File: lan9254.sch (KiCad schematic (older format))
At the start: 36 parts, among them U2301 lan9254, X2301 FNETHE025

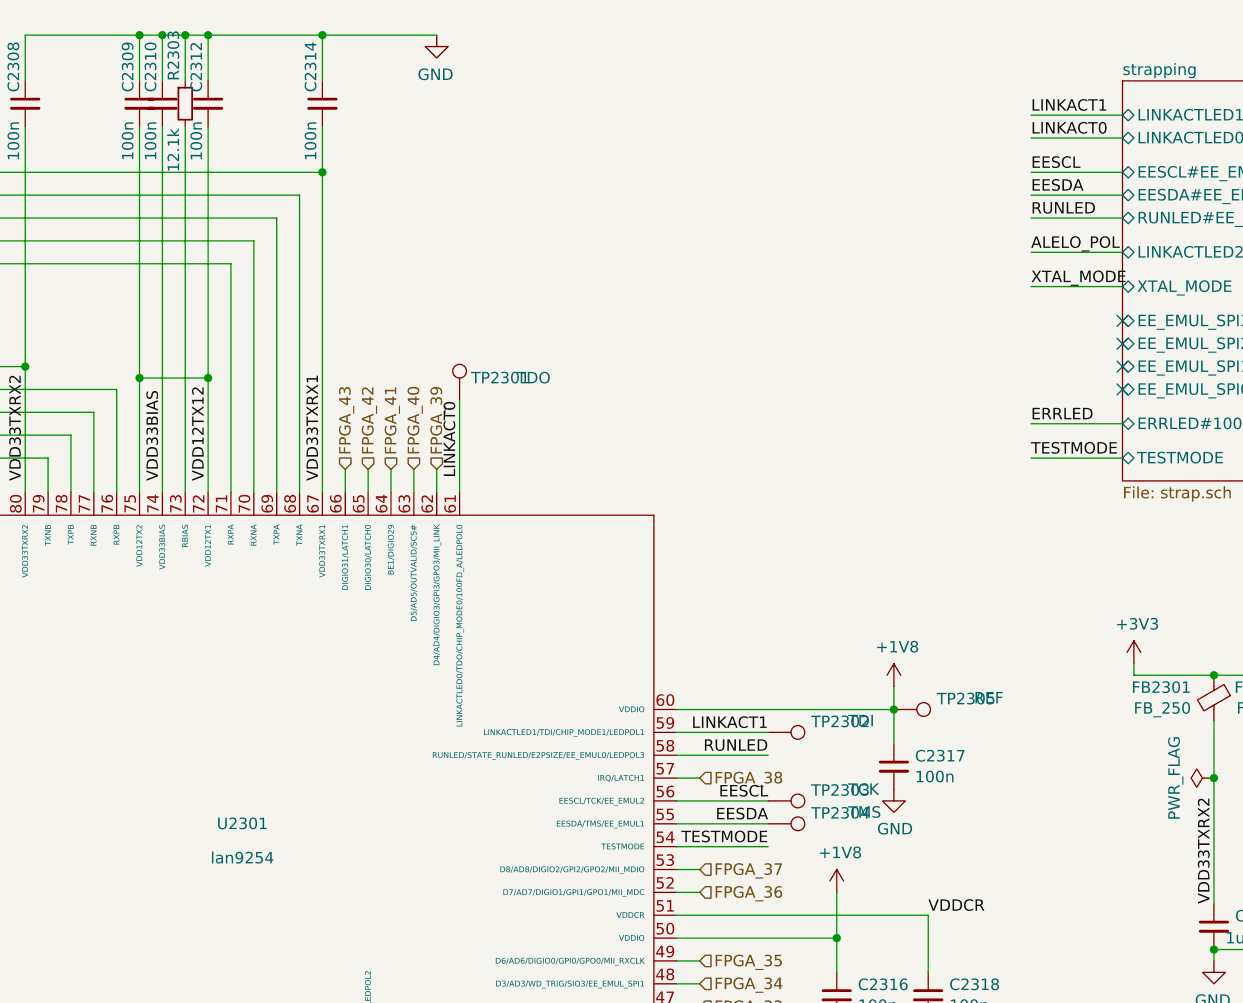
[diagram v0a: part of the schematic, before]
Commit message: fixed i2c switch (Vref2 is *not* a normal power input); small fixes
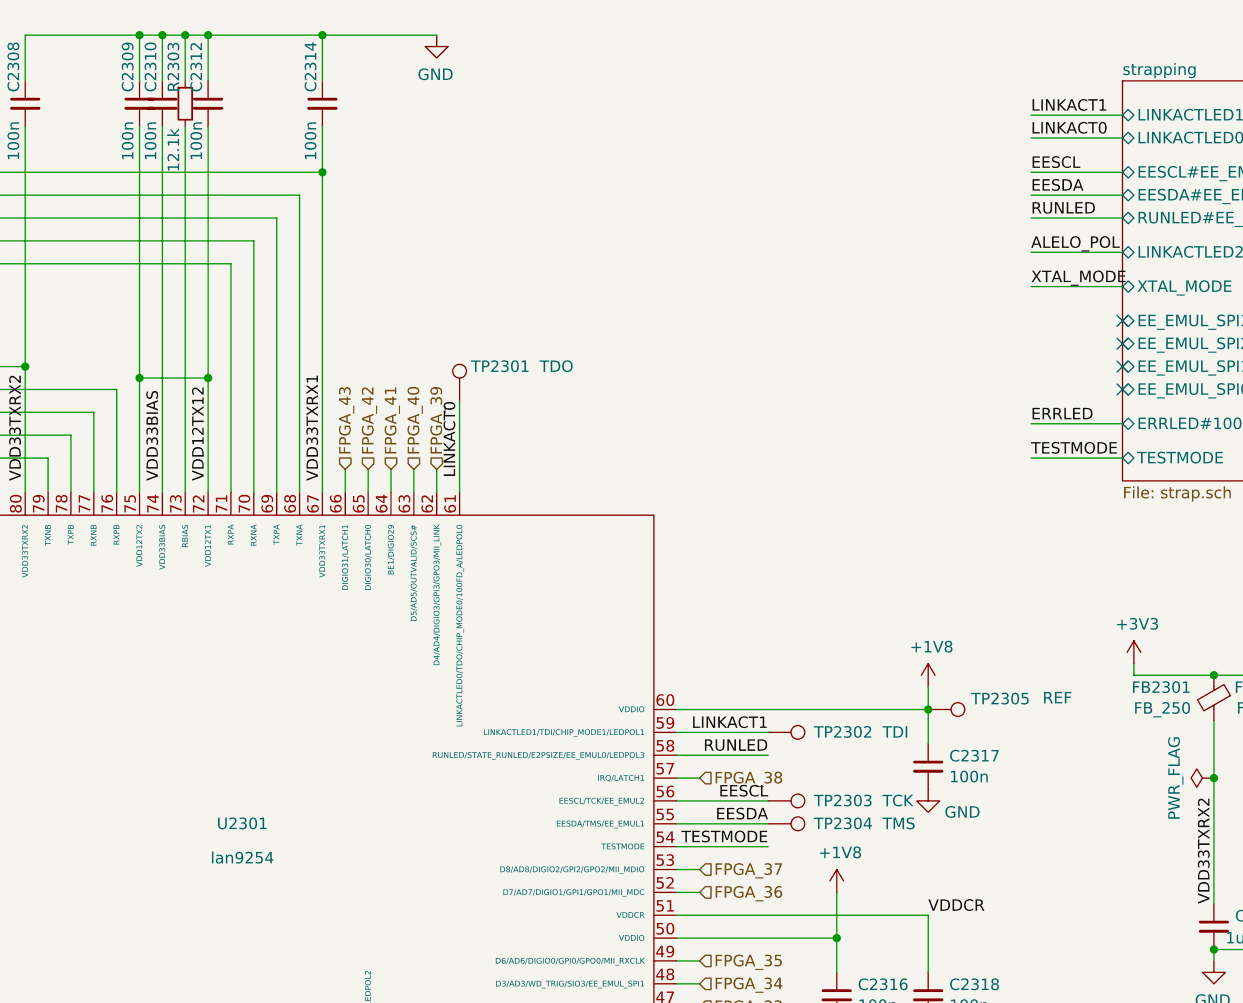
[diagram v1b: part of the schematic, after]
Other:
- moved on the sheet: C2317, TP2305
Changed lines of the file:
@@
 $Descr A4 11693 8268
 encoding utf-8
-Sheet 7 11
+Sheet 7 12
 Title ""
 Date ""
@@
 L Device:C_Small C2317
 U 1 1 60E78D0A
-P 7900 3800
-F 0 "C2317" H 7992 3846 50  0000 L CNN
-F 1 "100n" H 7992 3755 50  0000 L CNN
-F 2 "Capacitor_SMD:C_0402_1005Metric" H 7900 3800 50  0001 C CNN
-F 3 "~" H 7900 3800 50  0001 C CNN
-	1    7900 3800
+P 8050 3800
+F 0 "C2317" H 8142 3846 50  0000 L CNN
+F 1 "100n" H 8142 3755 50  0000 L CNN
+F 2 "Capacitor_SMD:C_0402_1005Metric" H 8050 3800 50  0001 C CNN
+F 3 "~" H 8050 3800 50  0001 C CNN
+	1    8050 3800
 	1    0    0    -1
 $EndComp
@@
 L lan9254_project:GND #PWR?
 U 1 1 60E78EE6
-P 7900 3900
+P 8050 3900
 AR Path="/60DC28BD/60E78EE6" Ref="#PWR?"  Part="1"
 AR Path="/60E78EE6" Ref="#PWR?"  Part="1"
 AR Path="/60DB2574/60E78EE6" Ref="#PWR?"  Part="1"
 AR Path="/60E70F2C/60E78EE6" Ref="#PWR?"  Part="1"
-F 0 "#PWR?" H 7900 3650 50  0001 C CNN
-F 1 "GND" H 7905 3727 50  0000 C CNN
-F 2 "" H 7900 3900 50  0001 C CNN
-F 3 "" H 7900 3900 50  0001 C CNN
-	1    7900 3900
-	1    0    0    -1
-$EndComp
-Wire Wire Line
-	7900 3550 7900 3700
+F 0 "#PWR?" H 8050 3650 50  0001 C CNN
+F 1 "GND" H 8200 3800 50  0000 C CNN
+F 2 "" H 8050 3900 50  0001 C CNN
+F 3 "" H 8050 3900 50  0001 C CNN
+	1    8050 3900
+	1    0    0    -1
+$EndComp
+Wire Wire Line
+	8050 3550 8050 3700
 $Comp
 L Device:C_Small C2307
@@
 L lan9254_project:+1V8 #PWR?
 U 1 1 60E92892
-P 7900 3450
+P 8050 3450
 AR Path="/60DC28BD/60E92892" Ref="#PWR?"  Part="1"
 AR Path="/60E92892" Ref="#PWR?"  Part="1"
 AR Path="/60DB2574/60E92892" Ref="#PWR?"  Part="1"
 AR Path="/60E70F2C/60E92892" Ref="#PWR?"  Part="1"
-F 0 "#PWR?" H 7900 3300 50  0001 C CNN
-F 1 "+1V8" H 7915 3623 50  0000 C CNN
-F 2 "" H 7900 3450 50  0001 C CNN
-F 3 "" H 7900 3450 50  0001 C CNN
-	1    7900 3450
-	1    0    0    -1
-$EndComp
-Wire Wire Line
-	7900 3450 7900 3550
-Connection ~ 7900 3550
+F 0 "#PWR?" H 8050 3300 50  0001 C CNN
+F 1 "+1V8" H 8065 3623 50  0000 C CNN
+F 2 "" H 8050 3450 50  0001 C CNN
+F 3 "" H 8050 3450 50  0001 C CNN
+	1    8050 3450
+	1    0    0    -1
+$EndComp
+Wire Wire Line
+	8050 3450 8050 3550
+Connection ~ 8050 3550
 $Comp
 L Device:C_Small C2306
@@
 AR Path="/60DB2574/60FA54A5" Ref="R2303"  Part="1"
 AR Path="/60E70F2C/60FA54A5" Ref="R2303"  Part="1"
-F 0 "R2303" V 4750 1000 50  0000 L CNN
+F 0 "R2303" V 4750 950 50  0000 L CNN
 F 1 "12.1k" V 4750 600 50  0000 L CNN
 F 2 "Resistor_SMD:R_0603_1608Metric" H 4800 900 50  0001 C CNN
@@
 U 1 1 60E57CD1
 P 6000 2200
-F 0 "TP2301" H 6050 2300 50  0000 L CNN
-F 1 "TDO" H 6250 2300 50  0000 L CNN
+F 0 "TP2301" H 6050 2350 50  0000 L CNN
+F 1 "TDO" H 6350 2350 50  0000 L CNN
 F 2 "Connector_PinHeader_1.27mm:PinHeader_1x01_P1.27mm_Vertical" H 6200 2200 50  0001 C CNN
 F 3 "~" H 6200 2200 50  0001 C CNN
@@
 U 1 1 60E58942
 P 7350 3650
-F 0 "TP2302" V 7304 3838 50  0000 L CNN
-F 1 "TDI" V 7300 4000 50  0000 L CNN
+F 0 "TP2302" V 7350 3850 50  0000 L CNN
+F 1 "TDI" V 7350 4150 50  0000 L CNN
 F 2 "Connector_PinHeader_1.27mm:PinHeader_1x01_P1.27mm_Vertical" H 7550 3650 50  0001 C CNN
 F 3 "~" H 7550 3650 50  0001 C CNN
@@
 	7650 4550 7650 4350
 Connection ~ 7650 4550
-Wire Wire Line
-	6950 3550 7900 3550
 $Comp
 L Connector:TestPoint TP2303
 U 1 1 60E83DE3
 P 7350 3950
-F 0 "TP2303" V 7304 4138 50  0000 L CNN
-F 1 "TCK" V 7300 4300 50  0000 L CNN
+F 0 "TP2303" V 7350 4150 50  0000 L CNN
+F 1 "TCK" V 7350 4450 50  0000 L CNN
 F 2 "Connector_PinHeader_1.27mm:PinHeader_1x01_P1.27mm_Vertical" H 7550 3950 50  0001 C CNN
 F 3 "~" H 7550 3950 50  0001 C CNN
@@
 U 1 1 60E841F7
 P 7350 4050
-F 0 "TP2304" V 7304 4238 50  0000 L CNN
-F 1 "TMS" V 7300 4400 50  0000 L CNN
+F 0 "TP2304" V 7350 4250 50  0000 L CNN
+F 1 "TMS" V 7350 4550 50  0000 L CNN
 F 2 "Connector_PinHeader_1.27mm:PinHeader_1x01_P1.27mm_Vertical" H 7550 4050 50  0001 C CNN
 F 3 "~" H 7550 4050 50  0001 C CNN
@@
 L Connector:TestPoint TP2305
 U 1 1 60E8477A
-P 7900 3550
-F 0 "TP2305" V 7854 3738 50  0000 L CNN
-F 1 "REF" V 7850 3900 50  0000 L CNN
-F 2 "Connector_PinHeader_1.27mm:PinHeader_1x01_P1.27mm_Vertical" H 8100 3550 50  0001 C CNN
-F 3 "~" H 8100 3550 50  0001 C CNN
-	1    7900 3550
+P 8050 3550
+F 0 "TP2305" V 8004 3738 50  0000 L CNN
+F 1 "REF" V 8000 4050 50  0000 L CNN
+F 2 "Connector_PinHeader_1.27mm:PinHeader_1x01_P1.27mm_Vertical" H 8250 3550 50  0001 C CNN
+F 3 "~" H 8250 3550 50  0001 C CNN
+	1    8050 3550
 	0    1    1    0
 $EndComp
+Wire Wire Line
+	6950 3550 8050 3550
 $EndSCHEMATC

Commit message: added more component values/part numbers
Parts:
- FB2301, FB2303, FB2304, FB4: Manufacturer (none) -> TDK
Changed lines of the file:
@@
 F 3 "~" H 9400 5350 50  0001 C CNN
 F 4 "MPZ1608S221ATA00" H 9400 5350 50  0001 C CNN "Part"
+F 5 "TDK" H 9400 5350 50  0001 C CNN "Manufacturer"
 	1    9400 5350
 	0    1    -1   0
@@
 F 3 "~" H 9300 3500 50  0001 C CNN
 F 4 "MPZ1608S221ATA00" H 9300 3500 50  0001 C CNN "Part"
+F 5 "TDK" H 9300 3500 50  0001 C CNN "Manufacturer"
 	1    9300 3500
 	-1   0    0    -1
@@
 F 3 "~" H 9750 3500 50  0001 C CNN
 F 4 "MPZ1608S221ATA00" H 9750 3500 50  0001 C CNN "Part"
+F 5 "TDK" H 9750 3500 50  0001 C CNN "Manufacturer"
 	1    9750 3500
 	-1   0    0    -1
@@
 F 3 "~" H 10200 3500 50  0001 C CNN
 F 4 "MPZ1608S221ATA00" H 10200 3500 50  0001 C CNN "Part"
+F 5 "TDK" H 10200 3500 50  0001 C CNN "Manufacturer"
 	1    10200 3500
 	-1   0    0    -1

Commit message: WIP save
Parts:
- added C2323: 100n, Capacitor_SMD:C_0603_1608Metric, symbol Device:C_Small
- added R2304: 50, Resistor_SMD:R_0603_1608Metric, symbol Device:R_Small
- added U2302: SN74LV1T34DBV, Package_TO_SOT_SMD:SOT-23-5, symbol Logic_LevelTranslator:SN74LV1T34DBV
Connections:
- net labels added: CLK_25MHz, CLK_25_VCC
- wire segments 195 -> 203
- no-connect marks 6 -> 7
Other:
- moved on the sheet: C2301, C2304
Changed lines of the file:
@@
 $Descr A4 11693 8268
 encoding utf-8
-Sheet 7 12
+Sheet 4 18
 Title ""
 Date ""
@@
 	1650 5400 1650 5450
 Wire Wire Line
-	1650 5450 2050 5450
+	1650 5450 1800 5450
 Connection ~ 2050 5450
 Wire Wire Line
@@
 L Device:C_Small C2304
 U 1 1 60EF9CC1
-P 1650 6250
-F 0 "C2304" H 1450 6300 50  0000 L CNN
-F 1 "1u_loESR" H 1250 6200 50  0000 L CNN
-F 2 "Capacitor_SMD:C_0603_1608Metric" H 1650 6250 50  0001 C CNN
-F 3 "~" H 1650 6250 50  0001 C CNN
-	1    1650 6250
+P 10950 5800
+F 0 "C2304" H 10750 5850 50  0000 L CNN
+F 1 "1u_loESR" H 10550 5750 50  0000 L CNN
+F 2 "Capacitor_SMD:C_0603_1608Metric" H 10950 5800 50  0001 C CNN
+F 3 "~" H 10950 5800 50  0001 C CNN
+	1    10950 5800
 	1    0    0    -1
 $EndComp
@@
 L lan9254_project:GND #PWR?
 U 1 1 60EFA87D
-P 1650 6450
+P 10950 6000
 AR Path="/60DC28BD/60EFA87D" Ref="#PWR?"  Part="1"
 AR Path="/60EFA87D" Ref="#PWR?"  Part="1"
 AR Path="/60DB2574/60EFA87D" Ref="#PWR?"  Part="1"
 AR Path="/60E70F2C/60EFA87D" Ref="#PWR?"  Part="1"
-F 0 "#PWR?" H 1650 6200 50  0001 C CNN
-F 1 "GND" H 1655 6277 50  0000 C CNN
-F 2 "" H 1650 6450 50  0001 C CNN
-F 3 "" H 1650 6450 50  0001 C CNN
-	1    1650 6450
+F 0 "#PWR?" H 10950 5750 50  0001 C CNN
+F 1 "GND" H 10955 5827 50  0000 C CNN
+F 2 "" H 10950 6000 50  0001 C CNN
+F 3 "" H 10950 6000 50  0001 C CNN
+	1    10950 6000
 	-1   0    0    -1
 $EndComp
 Wire Wire Line
-	1650 6350 1650 6450
+	10950 5900 10950 6000
 $Comp
 L lan9254_project:+3V3 #PWR?
 U 1 1 60F00E50
-P 1650 6050
+P 10950 5600
 AR Path="/60DC28BD/60F00E50" Ref="#PWR?"  Part="1"
 AR Path="/60F00E50" Ref="#PWR?"  Part="1"
 AR Path="/60DB2574/60F00E50" Ref="#PWR?"  Part="1"
 AR Path="/60E70F2C/60F00E50" Ref="#PWR?"  Part="1"
-F 0 "#PWR?" H 1650 5900 50  0001 C CNN
-F 1 "+3V3" H 1665 6223 50  0000 C CNN
-F 2 "" H 1650 6050 50  0001 C CNN
-F 3 "" H 1650 6050 50  0001 C CNN
-	1    1650 6050
-	1    0    0    -1
-$EndComp
-Wire Wire Line
-	1650 6050 1650 6150
+F 0 "#PWR?" H 10950 5450 50  0001 C CNN
+F 1 "+3V3" H 10965 5773 50  0000 C CNN
+F 2 "" H 10950 5600 50  0001 C CNN
+F 3 "" H 10950 5600 50  0001 C CNN
+	1    10950 5600
+	1    0    0    -1
+$EndComp
+Wire Wire Line
+	10950 5600 10950 5700
 $Comp
 L Device:C_Small C2301
 U 1 1 60F08215
-P 1000 6250
-F 0 "C2301" H 800 6300 50  0000 L CNN
-F 1 "1u_loESR" H 600 6200 50  0000 L CNN
-F 2 "Capacitor_SMD:C_0603_1608Metric" H 1000 6250 50  0001 C CNN
-F 3 "~" H 1000 6250 50  0001 C CNN
-	1    1000 6250
+P 10300 5800
+F 0 "C2301" H 10100 5850 50  0000 L CNN
+F 1 "1u_loESR" H 9900 5750 50  0000 L CNN
+F 2 "Capacitor_SMD:C_0603_1608Metric" H 10300 5800 50  0001 C CNN
+F 3 "~" H 10300 5800 50  0001 C CNN
+	1    10300 5800
 	1    0    0    -1
 $EndComp
@@
 L lan9254_project:GND #PWR?
 U 1 1 60F084D9
-P 1000 6450
+P 10300 6000
 AR Path="/60DC28BD/60F084D9" Ref="#PWR?"  Part="1"
 AR Path="/60F084D9" Ref="#PWR?"  Part="1"
 AR Path="/60DB2574/60F084D9" Ref="#PWR?"  Part="1"
 AR Path="/60E70F2C/60F084D9" Ref="#PWR?"  Part="1"
-F 0 "#PWR?" H 1000 6200 50  0001 C CNN
-F 1 "GND" H 1005 6277 50  0000 C CNN
-F 2 "" H 1000 6450 50  0001 C CNN
-F 3 "" H 1000 6450 50  0001 C CNN
-	1    1000 6450
+F 0 "#PWR?" H 10300 5750 50  0001 C CNN
+F 1 "GND" H 10305 5827 50  0000 C CNN
+F 2 "" H 10300 6000 50  0001 C CNN
+F 3 "" H 10300 6000 50  0001 C CNN
+	1    10300 6000
 	-1   0    0    -1
 $EndComp
 Wire Wire Line
-	1000 6350 1000 6450
-Wire Wire Line
-	1000 6050 1000 6150
+	10300 5900 10300 6000
+Wire Wire Line
+	10300 5600 10300 5700
 $Comp
 L lan9254_project:+1V8 #PWR?
 U 1 1 60F0F989
-P 1000 6050
+P 10300 5600
 AR Path="/60DC28BD/60F0F989" Ref="#PWR?"  Part="1"
 AR Path="/60F0F989" Ref="#PWR?"  Part="1"
 AR Path="/60DB2574/60F0F989" Ref="#PWR?"  Part="1"
 AR Path="/60E70F2C/60F0F989" Ref="#PWR?"  Part="1"
-F 0 "#PWR?" H 1000 5900 50  0001 C CNN
-F 1 "+1V8" H 1015 6223 50  0000 C CNN
-F 2 "" H 1000 6050 50  0001 C CNN
-F 3 "" H 1000 6050 50  0001 C CNN
-	1    1000 6050
+F 0 "#PWR?" H 10300 5450 50  0001 C CNN
+F 1 "+1V8" H 10315 5773 50  0000 C CNN
+F 2 "" H 10300 5600 50  0001 C CNN
+F 3 "" H 10300 5600 50  0001 C CNN
+	1    10300 5600
 	1    0    0    -1
 $EndComp
@@
 Wire Wire Line
 	8900 1050 8500 1050
-Text Label 8500 1050 0    50   ~ 0
-LINKACT0
 $Sheet
 S 8900 800  1550 1750
@@
 Connection ~ 1800 3850
 $Sheet
-S 1800 7200 550  300
+S 7500 1250 550  300
 U 60EF9F81
 F0 "IO_driver_1" 50
 F1 "IO_driver.sch" 50
-F2 "DATA" B L 1800 7350 50
-F3 "DIR" I L 1800 7250 50
+F2 "DATA" B L 7500 1400 50
+F3 "DIR" I L 7500 1300 50
 $EndSheet
 $Sheet
-S 3200 7200 550  300
+S 7500 1950 550  300
 U 60E556C7
 F0 "IO_driver_2" 50
 F1 "IO_driver.sch" 50
-F2 "DATA" B L 3200 7350 50
-F3 "DIR" I L 3200 7250 50
+F2 "DATA" B L 7500 2100 50
+F3 "DIR" I L 7500 2000 50
 $EndSheet
-Text HLabel 3100 7250 0    50   Input ~ 0
+Text HLabel 7400 2000 0    50   Input ~ 0
 FPGA_IO2_DIR
-Text HLabel 3100 7350 0    50   BiDi ~ 0
+Text HLabel 7400 2100 0    50   BiDi ~ 0
 FPGA_IO2_DAT
-Text HLabel 1700 7350 0    50   BiDi ~ 0
+Text HLabel 7400 1400 0    50   BiDi ~ 0
 FPGA_IO1_DAT
-Text HLabel 1700 7250 0    50   Input ~ 0
+Text HLabel 7400 1300 0    50   Input ~ 0
 FPGA_IO1_DIR
 Wire Wire Line
-	1700 7350 1800 7350
-Wire Wire Line
-	1700 7250 1800 7250
-Wire Wire Line
-	3100 7250 3200 7250
-Wire Wire Line
-	3100 7350 3200 7350
+	7400 1400 7500 1400
+Wire Wire Line
+	7400 1300 7500 1300
+Wire Wire Line
+	7400 2000 7500 2000
+Wire Wire Line
+	7400 2100 7500 2100
 $Comp
 L Connector:TestPoint TP2301
@@
 Wire Wire Line
 	6950 3550 8050 3550
+NoConn ~ 8500 1050
+$Comp
+L Logic_LevelTranslator:SN74LV1T34DBV U2302
+U 1 1 61FE5B40
+P 1800 6500
+F 0 "U2302" H 2050 6900 50  0000 R CNN
+F 1 "SN74LV1T34DBV" H 2050 7000 50  0000 R CNN
+F 2 "Package_TO_SOT_SMD:SOT-23-5" H 2450 6250 50  0001 C CNN
+F 3 "https://www.ti.com/lit/ds/symlink/sn74lv1t34.pdf" H 1400 6300 50  0001 C CNN
+	1    1800 6500
+	-1   0    0    1
+$EndComp
+$Comp
+L Device:C_Small C2323
+U 1 1 61FE65E4
+P 1800 5900
+F 0 "C2323" H 1892 5946 50  0000 L CNN
+F 1 "100n" H 1892 5855 50  0000 L CNN
+F 2 "Capacitor_SMD:C_0603_1608Metric" H 1800 5900 50  0001 C CNN
+F 3 "~" H 1800 5900 50  0001 C CNN
+	1    1800 5900
+	-1   0    0    -1
+$EndComp
+Text Label 2300 6500 1    50   ~ 0
+XTAL_MODE
+$Comp
+L lan9254_project:GND #PWR?
+U 1 1 61FF1A93
+P 1800 6800
+AR Path="/60DC28BD/61FF1A93" Ref="#PWR?"  Part="1"
+AR Path="/61FF1A93" Ref="#PWR?"  Part="1"
+AR Path="/60DB2574/61FF1A93" Ref="#PWR?"  Part="1"
+AR Path="/60E70F2C/61FF1A93" Ref="#PWR?"  Part="1"
+F 0 "#PWR?" H 1800 6550 50  0001 C CNN
+F 1 "GND" H 1805 6627 50  0001 C CNN
+F 2 "" H 1800 6800 50  0001 C CNN
+F 3 "" H 1800 6800 50  0001 C CNN
+	1    1800 6800
+	1    0    0    -1
+$EndComp
+Text HLabel 1200 6500 0    50   Output ~ 0
+CLK_25MHz
+Wire Wire Line
+	2300 6500 2100 6500
+$Comp
+L Device:R_Small R?
+U 1 1 62066CC1
+P 1350 6500
+AR Path="/60DC28BD/62066CC1" Ref="R?"  Part="1"
+AR Path="/62066CC1" Ref="R?"  Part="1"
+AR Path="/60DB2574/62066CC1" Ref="R?"  Part="1"
+AR Path="/60E70F2C/62066CC1" Ref="R2304"  Part="1"
+F 0 "R2304" H 1409 6546 50  0000 L CNN
+F 1 "50" H 1409 6455 50  0000 L CNN
+F 2 "Resistor_SMD:R_0603_1608Metric" H 1350 6500 50  0001 C CNN
+F 3 "~" H 1350 6500 50  0001 C CNN
+	1    1350 6500
+	0    1    1    0
+$EndComp
+Wire Wire Line
+	1800 5800 1800 5450
+Connection ~ 1800 5450
+Wire Wire Line
+	1800 5450 2050 5450
+Wire Wire Line
+	1800 6000 1800 6100
+Wire Wire Line
+	1200 6500 1250 6500
+Wire Wire Line
+	1450 6500 1500 6500
+Text HLabel 1200 6100 0    50   Input ~ 0
+CLK_25_VCC
+Wire Wire Line
+	1200 6100 1800 6100
+Connection ~ 1800 6100
+Wire Wire Line
+	1800 6100 1800 6200
 $EndSCHEMATC

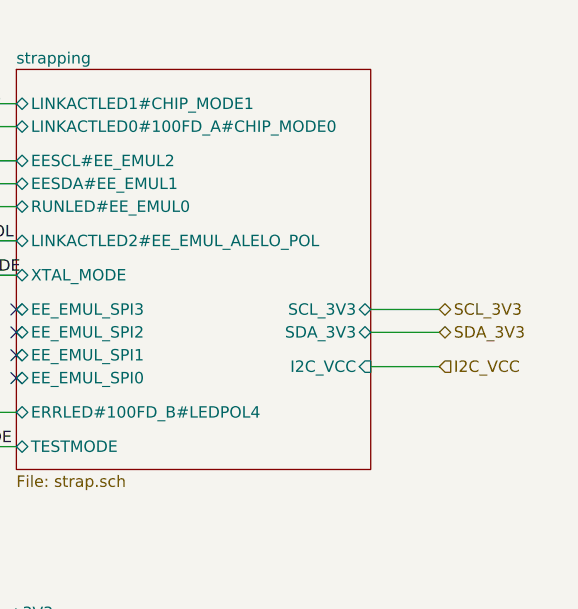
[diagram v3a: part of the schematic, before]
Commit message: changed LED drivers; added Jumpers, write-protect
Modified LED drivers (XOR approach) to work with lan9254's
open-drain/-source outputs.

Routed spare switches as jumpers out of this module.

Route eeprom-write protect out of this module.
Route eeprom-isolation switch info out (so that FPGA may easily
determine whether EEPROM emulation is used or not).
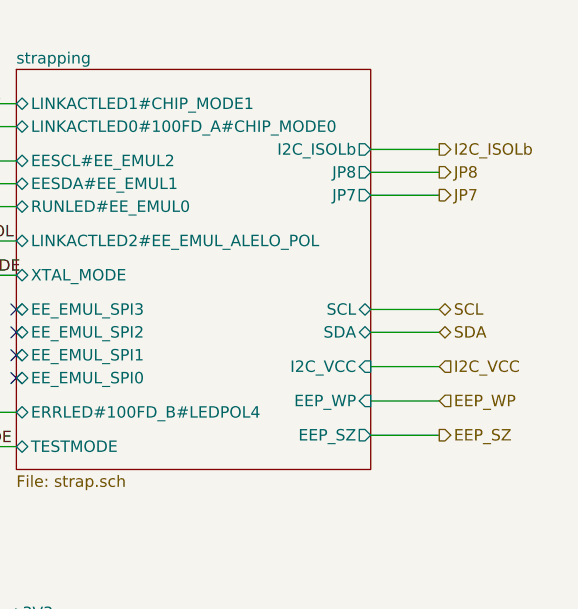
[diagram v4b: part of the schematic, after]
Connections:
- net labels added: EEP_SZ, EEP_WP, I2C_ISOLb, JP7, JP8, SCL, SDA
- net labels removed: SCL_3V3, SDA_3V3
- wire segments 203 -> 208
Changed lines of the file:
@@
 $Descr A4 11693 8268
 encoding utf-8
-Sheet 4 18
+Sheet 13 18
 Title ""
 Date ""
@@
 	10450 1950 10750 1950
 Text HLabel 10750 1950 2    50   BiDi ~ 0
-SDA_3V3
+SDA
 Text HLabel 10750 1850 2    50   BiDi ~ 0
-SCL_3V3
+SCL
 NoConn ~ 8900 1850
 NoConn ~ 8900 1950
@@
 F12 "LINKACTLED2#EE_EMUL_ALELO_POL" B L 8900 1550 50
 F13 "ERRLED#100FD_B#LEDPOL4" B L 8900 2300 50
-F14 "SCL_3V3" B R 10450 1850 50
-F15 "SDA_3V3" B R 10450 1950 50
-F16 "TESTMODE" B L 8900 2450 50
-F17 "I2C_VCC" I R 10450 2100 50
+F14 "TESTMODE" B L 8900 2450 50
+F15 "I2C_VCC" I R 10450 2100 50
+F16 "I2C_ISOLb" O R 10450 1150 50
+F17 "JP8" O R 10450 1250 50
+F18 "JP7" O R 10450 1350 50
+F19 "SCL" B R 10450 1850 50
+F20 "SDA" B R 10450 1950 50
+F21 "EEP_WP" I R 10450 2250 50
+F22 "EEP_SZ" O R 10450 2400 50
 $EndSheet
 Wire Wire Line
@@
 Wire Wire Line
 	1800 6100 1800 6200
+Text HLabel 10750 1150 2    50   Output ~ 0
+I2C_ISOLb
+Text HLabel 10750 1250 2    50   Output ~ 0
+JP8
+Text HLabel 10750 1350 2    50   Output ~ 0
+JP7
+Wire Wire Line
+	10450 1150 10750 1150
+Wire Wire Line
+	10450 1250 10750 1250
+Wire Wire Line
+	10450 1350 10750 1350
+Text HLabel 10750 2250 2    50   Input ~ 0
+EEP_WP
+Wire Wire Line
+	10450 2250 10750 2250
+Text HLabel 10750 2400 2    50   Output ~ 0
+EEP_SZ
+Wire Wire Line
+	10750 2400 10450 2400
 $EndSCHEMATC
